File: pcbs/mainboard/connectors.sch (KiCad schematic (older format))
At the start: 10 parts, among them J10 STAT_LED, J11 nReset_Button, J2 key_row_0, J3 key_row_1, J4 key_row_2, J5 ICSP, J6 JTAG, J7 Crank, J8 GPIO, J9 I2C

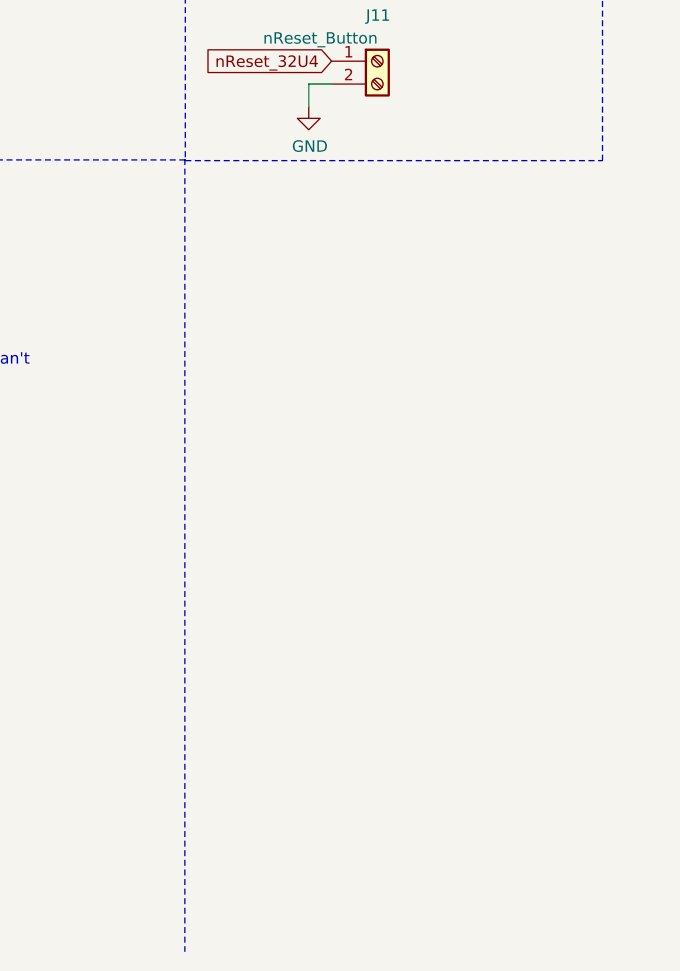
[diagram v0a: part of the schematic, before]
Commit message: Add mounting holes and fix button footprint
Replace button footprint with one which matches the symbol.
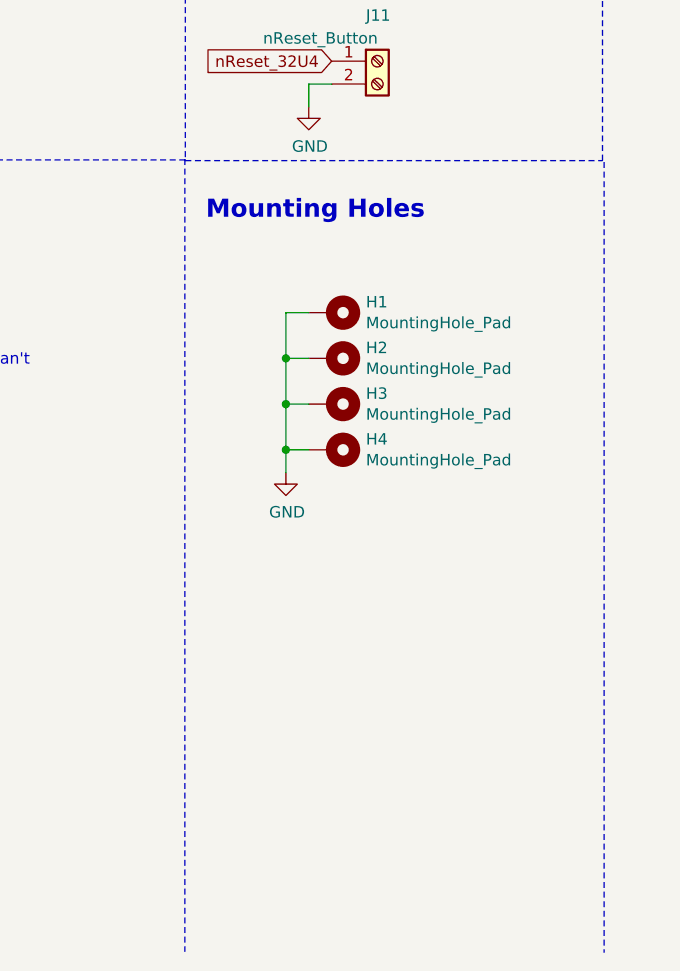
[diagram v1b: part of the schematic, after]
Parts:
- added H1, H2, H3, H4: MountingHole_Pad, MountingHole:MountingHole_3.2mm_M3_Pad_Via, symbol Mechanical:MountingHole_Pad
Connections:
- wire segments 17 -> 25
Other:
- note added: "Mounting Holes"
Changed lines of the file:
@@
 Wire Wire Line
 	1250 6900 1300 6900
+Wire Notes Line
+	4942 4341 4942 7800
+Text Notes 3200 4600 0    79   ~ 16
+Mounting Holes
+$Comp
+L Mechanical:MountingHole_Pad H1
+U 1 1 6153CC4B
+P 3750 5000
+F 0 "H1" V 3704 5150 50  0000 L CNN
+F 1 "MountingHole_Pad" V 3795 5150 50  0000 L CNN
+F 2 "MountingHole:MountingHole_3.2mm_M3_Pad_Via" H 3750 5000 50  0001 C CNN
+F 3 "~" H 3750 5000 50  0001 C CNN
+	1    3750 5000
+	0    1    1    0
+$EndComp
+$Comp
+L Mechanical:MountingHole_Pad H2
+U 1 1 6153E1D0
+P 3750 5200
+F 0 "H2" V 3704 5350 50  0000 L CNN
+F 1 "MountingHole_Pad" V 3795 5350 50  0000 L CNN
+F 2 "MountingHole:MountingHole_3.2mm_M3_Pad_Via" H 3750 5200 50  0001 C CNN
+F 3 "~" H 3750 5200 50  0001 C CNN
+	1    3750 5200
+	0    1    1    0
+$EndComp
+$Comp
+L Mechanical:MountingHole_Pad H3
+U 1 1 6153E50B
+P 3750 5400
+F 0 "H3" V 3704 5550 50  0000 L CNN
+F 1 "MountingHole_Pad" V 3795 5550 50  0000 L CNN
+F 2 "MountingHole:MountingHole_3.2mm_M3_Pad_Via" H 3750 5400 50  0001 C CNN
+F 3 "~" H 3750 5400 50  0001 C CNN
+	1    3750 5400
+	0    1    1    0
+$EndComp
+$Comp
+L Mechanical:MountingHole_Pad H4
+U 1 1 6153E7C0
+P 3750 5600
+F 0 "H4" V 3704 5750 50  0000 L CNN
+F 1 "MountingHole_Pad" V 3795 5750 50  0000 L CNN
+F 2 "MountingHole:MountingHole_3.2mm_M3_Pad_Via" H 3750 5600 50  0001 C CNN
+F 3 "~" H 3750 5600 50  0001 C CNN
+	1    3750 5600
+	0    1    1    0
+$EndComp
+$Comp
+L power:GND #PWR0115
+U 1 1 6153EF14
+P 3550 5700
+F 0 "#PWR0115" H 3550 5450 50  0001 C CNN
+F 1 "GND" H 3555 5527 50  0000 C CNN
+F 2 "" H 3550 5700 50  0001 C CNN
+F 3 "" H 3550 5700 50  0001 C CNN
+	1    3550 5700
+	1    0    0    -1
+$EndComp
+Wire Wire Line
+	3550 5700 3550 5600
+Wire Wire Line
+	3550 5000 3650 5000
+Wire Wire Line
+	3650 5200 3550 5200
+Connection ~ 3550 5200
+Wire Wire Line
+	3550 5200 3550 5000
+Wire Wire Line
+	3550 5400 3650 5400
+Connection ~ 3550 5400
+Wire Wire Line
+	3550 5400 3550 5200
+Wire Wire Line
+	3650 5600 3550 5600
+Connection ~ 3550 5600
+Wire Wire Line
+	3550 5600 3550 5400
 $EndSCHEMATC

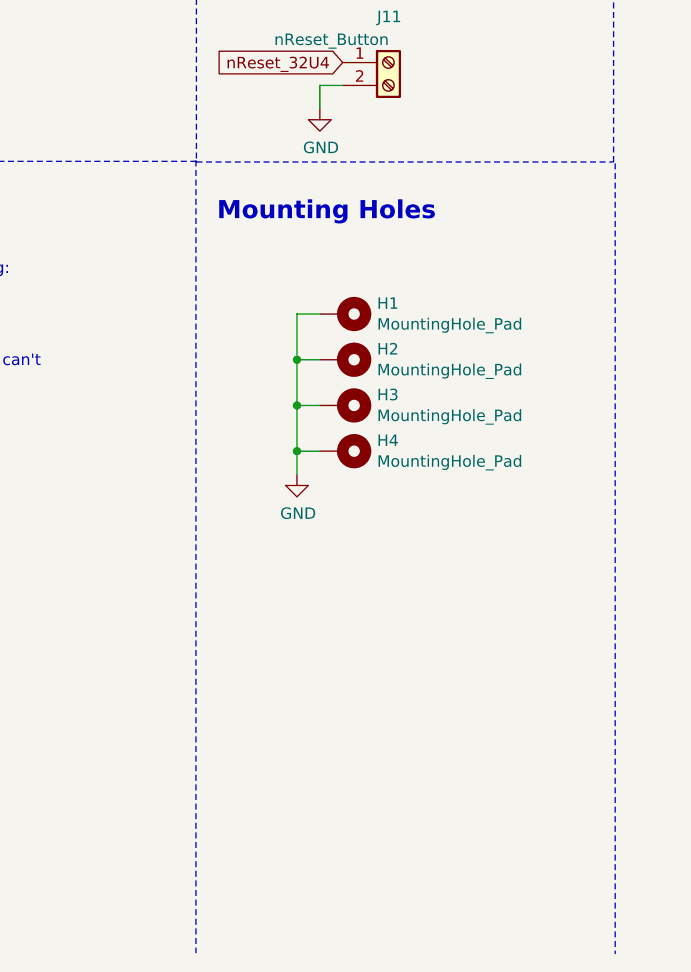
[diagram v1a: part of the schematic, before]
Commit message: Add VBUS screw terminal
Add VBUS screw terminal to allow future subsystems to draw current
from the USB connection, bypassing the small 3V3 regulator.
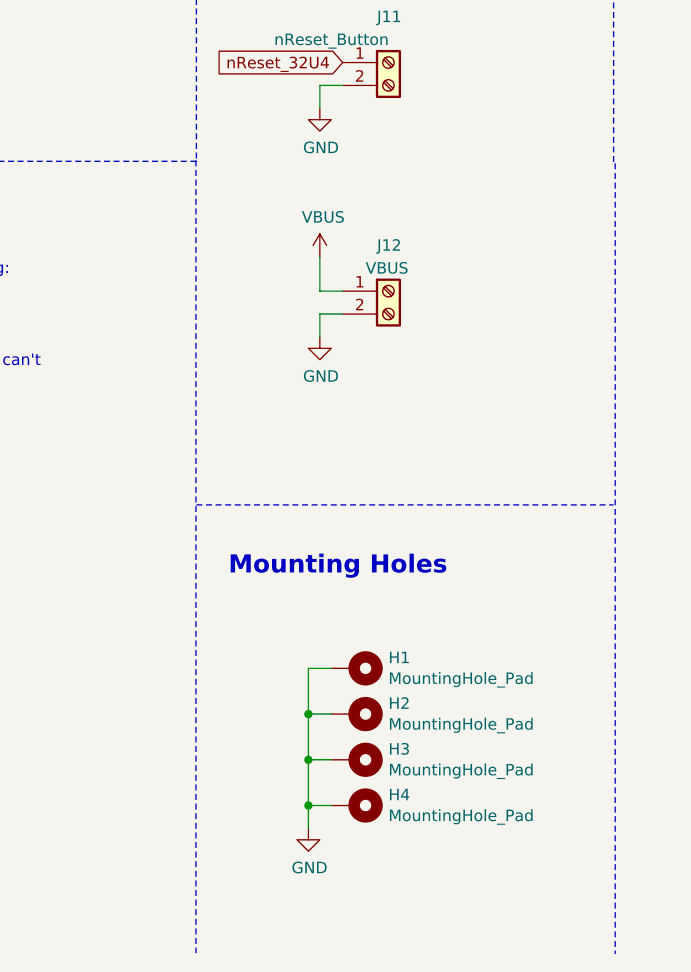
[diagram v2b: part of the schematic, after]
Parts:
- added J12: VBUS, TerminalBlock_Phoenix:TerminalBlock_Phoenix_MKDS-1,5-2-5.08_1x02_P5.08mm_Horizontal, symbol Connector:Screw_Terminal_01x02
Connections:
- net labels added: VBUS
- wire segments 25 -> 29
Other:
- moved on the sheet: H1, H2, H3, H4
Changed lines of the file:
@@
 $EndComp
 Wire Notes Line
-	3110 4335 4935 4335
+	3110 5835 4935 5835
 Wire Notes Line
 	4935 4335 4935 475
@@
 Wire Notes Line
 	4942 4341 4942 7800
-Text Notes 3200 4600 0    79   ~ 16
+Text Notes 3250 6150 0    79   ~ 16
 Mounting Holes
 $Comp
 L Mechanical:MountingHole_Pad H1
 U 1 1 6153CC4B
-P 3750 5000
-F 0 "H1" V 3704 5150 50  0000 L CNN
-F 1 "MountingHole_Pad" V 3795 5150 50  0000 L CNN
-F 2 "MountingHole:MountingHole_3.2mm_M3_Pad_Via" H 3750 5000 50  0001 C CNN
-F 3 "~" H 3750 5000 50  0001 C CNN
-	1    3750 5000
+P 3800 6550
+F 0 "H1" V 3754 6700 50  0000 L CNN
+F 1 "MountingHole_Pad" V 3845 6700 50  0000 L CNN
+F 2 "MountingHole:MountingHole_3.2mm_M3_Pad_Via" H 3800 6550 50  0001 C CNN
+F 3 "~" H 3800 6550 50  0001 C CNN
+	1    3800 6550
 	0    1    1    0
 $EndComp
@@
 L Mechanical:MountingHole_Pad H2
 U 1 1 6153E1D0
-P 3750 5200
-F 0 "H2" V 3704 5350 50  0000 L CNN
-F 1 "MountingHole_Pad" V 3795 5350 50  0000 L CNN
-F 2 "MountingHole:MountingHole_3.2mm_M3_Pad_Via" H 3750 5200 50  0001 C CNN
-F 3 "~" H 3750 5200 50  0001 C CNN
-	1    3750 5200
+P 3800 6750
+F 0 "H2" V 3754 6900 50  0000 L CNN
+F 1 "MountingHole_Pad" V 3845 6900 50  0000 L CNN
+F 2 "MountingHole:MountingHole_3.2mm_M3_Pad_Via" H 3800 6750 50  0001 C CNN
+F 3 "~" H 3800 6750 50  0001 C CNN
+	1    3800 6750
 	0    1    1    0
 $EndComp
@@
 L Mechanical:MountingHole_Pad H3
 U 1 1 6153E50B
-P 3750 5400
-F 0 "H3" V 3704 5550 50  0000 L CNN
-F 1 "MountingHole_Pad" V 3795 5550 50  0000 L CNN
-F 2 "MountingHole:MountingHole_3.2mm_M3_Pad_Via" H 3750 5400 50  0001 C CNN
-F 3 "~" H 3750 5400 50  0001 C CNN
-	1    3750 5400
+P 3800 6950
+F 0 "H3" V 3754 7100 50  0000 L CNN
+F 1 "MountingHole_Pad" V 3845 7100 50  0000 L CNN
+F 2 "MountingHole:MountingHole_3.2mm_M3_Pad_Via" H 3800 6950 50  0001 C CNN
+F 3 "~" H 3800 6950 50  0001 C CNN
+	1    3800 6950
 	0    1    1    0
 $EndComp
@@
 L Mechanical:MountingHole_Pad H4
 U 1 1 6153E7C0
-P 3750 5600
-F 0 "H4" V 3704 5750 50  0000 L CNN
-F 1 "MountingHole_Pad" V 3795 5750 50  0000 L CNN
-F 2 "MountingHole:MountingHole_3.2mm_M3_Pad_Via" H 3750 5600 50  0001 C CNN
-F 3 "~" H 3750 5600 50  0001 C CNN
-	1    3750 5600
+P 3800 7150
+F 0 "H4" V 3754 7300 50  0000 L CNN
+F 1 "MountingHole_Pad" V 3845 7300 50  0000 L CNN
+F 2 "MountingHole:MountingHole_3.2mm_M3_Pad_Via" H 3800 7150 50  0001 C CNN
+F 3 "~" H 3800 7150 50  0001 C CNN
+	1    3800 7150
 	0    1    1    0
 $EndComp
@@
 L power:GND #PWR0115
 U 1 1 6153EF14
-P 3550 5700
-F 0 "#PWR0115" H 3550 5450 50  0001 C CNN
-F 1 "GND" H 3555 5527 50  0000 C CNN
-F 2 "" H 3550 5700 50  0001 C CNN
-F 3 "" H 3550 5700 50  0001 C CNN
-	1    3550 5700
-	1    0    0    -1
-$EndComp
-Wire Wire Line
-	3550 5700 3550 5600
-Wire Wire Line
-	3550 5000 3650 5000
-Wire Wire Line
-	3650 5200 3550 5200
-Connection ~ 3550 5200
-Wire Wire Line
-	3550 5200 3550 5000
-Wire Wire Line
-	3550 5400 3650 5400
-Connection ~ 3550 5400
-Wire Wire Line
-	3550 5400 3550 5200
-Wire Wire Line
-	3650 5600 3550 5600
-Connection ~ 3550 5600
-Wire Wire Line
-	3550 5600 3550 5400
+P 3600 7250
+F 0 "#PWR0115" H 3600 7000 50  0001 C CNN
+F 1 "GND" H 3605 7077 50  0000 C CNN
+F 2 "" H 3600 7250 50  0001 C CNN
+F 3 "" H 3600 7250 50  0001 C CNN
+	1    3600 7250
+	1    0    0    -1
+$EndComp
+Wire Wire Line
+	3600 7250 3600 7150
+Wire Wire Line
+	3600 6550 3700 6550
+Wire Wire Line
+	3700 6750 3600 6750
+Connection ~ 3600 6750
+Wire Wire Line
+	3600 6750 3600 6550
+Wire Wire Line
+	3600 6950 3700 6950
+Connection ~ 3600 6950
+Wire Wire Line
+	3600 6950 3600 6750
+Wire Wire Line
+	3700 7150 3600 7150
+Connection ~ 3600 7150
+Wire Wire Line
+	3600 7150 3600 6950
+Wire Wire Line
+	3650 5000 3750 5000
+Wire Wire Line
+	3650 5100 3650 5000
+$Comp
+L power:GND #PWR0116
+U 1 1 61620CEB
+P 3650 5100
+F 0 "#PWR0116" H 3650 4850 50  0001 C CNN
+F 1 "GND" H 3655 4927 50  0000 C CNN
+F 2 "" H 3650 5100 50  0001 C CNN
+F 3 "" H 3650 5100 50  0001 C CNN
+	1    3650 5100
+	1    0    0    -1
+$EndComp
+$Comp
+L Connector:Screw_Terminal_01x02 J12
+U 1 1 61620CF5
+P 3950 4900
+F 0 "J12" H 3900 5100 50  0000 L CNN
+F 1 "VBUS" H 3850 5000 50  0000 L CNN
+F 2 "TerminalBlock_Phoenix:TerminalBlock_Phoenix_MKDS-1,5-2-5.08_1x02_P5.08mm_Horizontal" H 3950 4900 50  0001 C CNN
+F 3 "~" H 3950 4900 50  0001 C CNN
+	1    3950 4900
+	1    0    0    -1
+$EndComp
+$Comp
+L power:VBUS #PWR0117
+U 1 1 616267BA
+P 3650 4750
+F 0 "#PWR0117" H 3650 4600 50  0001 C CNN
+F 1 "VBUS" H 3665 4923 50  0000 C CNN
+F 2 "" H 3650 4750 50  0001 C CNN
+F 3 "" H 3650 4750 50  0001 C CNN
+	1    3650 4750
+	1    0    0    -1
+$EndComp
+Wire Wire Line
+	3650 4750 3650 4900
+Wire Wire Line
+	3650 4900 3750 4900
 $EndSCHEMATC

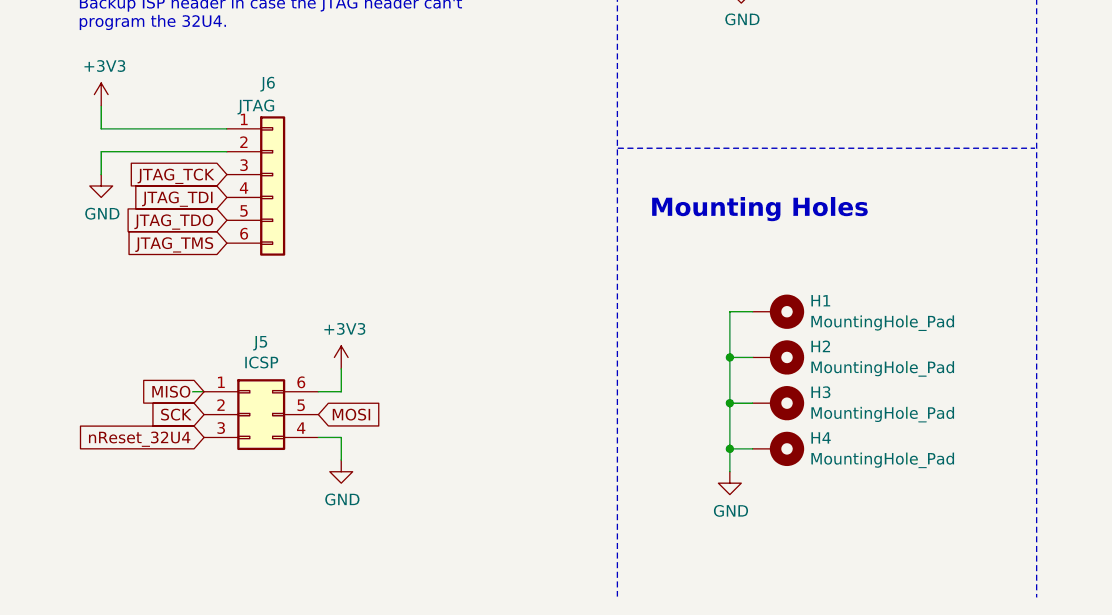
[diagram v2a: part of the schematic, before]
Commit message: Add first draft of mainboard layout
Change pinout of XC95 to better link to the key_row screw terminals.

Change ordering of some signals on screw terminals and JTAG header
to allow more sensible routing.

Revise mounting hole scheme to only place one between the two rows
of terminal blocks rather than at each corner on the top.
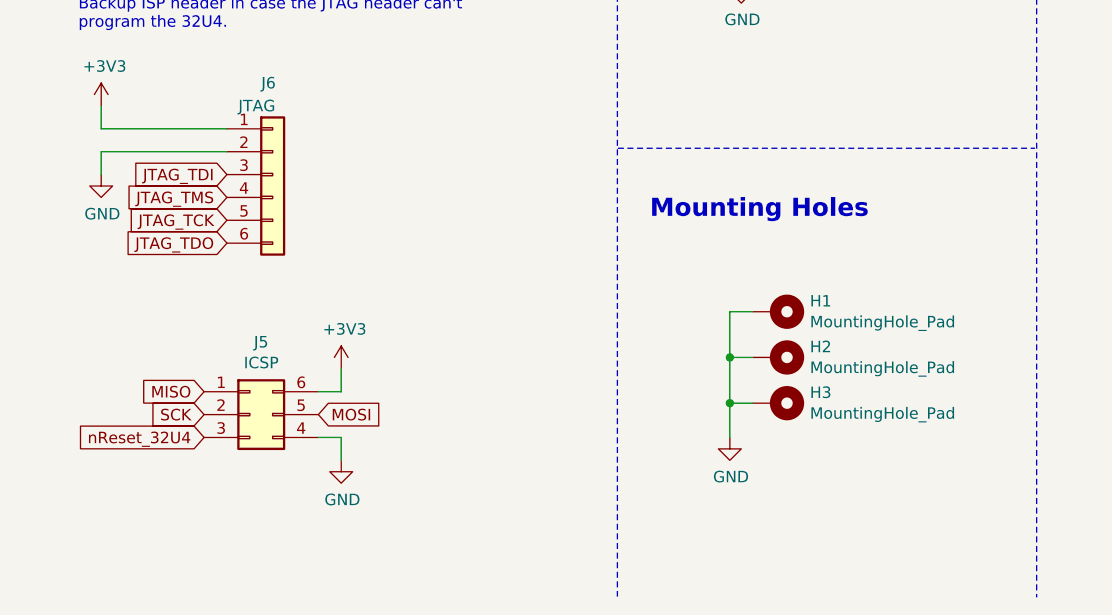
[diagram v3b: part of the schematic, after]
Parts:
- removed H4: MountingHole_Pad, MountingHole:MountingHole_3.2mm_M3_Pad_Via, symbol Mechanical:MountingHole_Pad
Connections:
- wire segments 29 -> 26
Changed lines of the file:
@@
 Wire Wire Line
 	850  5750 1400 5750
+Text GLabel 1400 6150 0    50   Input ~ 0
+JTAG_TCK
 Text GLabel 1400 5950 0    50   Input ~ 0
-JTAG_TCK
+JTAG_TDI
+Text GLabel 1400 6250 0    50   Input ~ 0
+JTAG_TDO
 Text GLabel 1400 6050 0    50   Input ~ 0
-JTAG_TDI
-Text GLabel 1400 6150 0    50   Input ~ 0
-JTAG_TDO
-Text GLabel 1400 6250 0    50   Input ~ 0
 JTAG_TMS
 Text GLabel 1300 7100 0    50   Input ~ 0
@@
 	1    0    0    -1
 $EndComp
-Wire Wire Line
-	1250 6900 1300 6900
 Wire Notes Line
 	4942 4341 4942 7800
@@
 $EndComp
 $Comp
-L Mechanical:MountingHole_Pad H4
-U 1 1 6153E7C0
-P 3800 7150
-F 0 "H4" V 3754 7300 50  0000 L CNN
-F 1 "MountingHole_Pad" V 3845 7300 50  0000 L CNN
-F 2 "MountingHole:MountingHole_3.2mm_M3_Pad_Via" H 3800 7150 50  0001 C CNN
-F 3 "~" H 3800 7150 50  0001 C CNN
-	1    3800 7150
-	0    1    1    0
-$EndComp
-$Comp
 L power:GND #PWR0115
 U 1 1 6153EF14
-P 3600 7250
-F 0 "#PWR0115" H 3600 7000 50  0001 C CNN
-F 1 "GND" H 3605 7077 50  0000 C CNN
-F 2 "" H 3600 7250 50  0001 C CNN
-F 3 "" H 3600 7250 50  0001 C CNN
-	1    3600 7250
-	1    0    0    -1
-$EndComp
-Wire Wire Line
-	3600 7250 3600 7150
+P 3600 7100
+F 0 "#PWR0115" H 3600 6850 50  0001 C CNN
+F 1 "GND" H 3605 6927 50  0000 C CNN
+F 2 "" H 3600 7100 50  0001 C CNN
+F 3 "" H 3600 7100 50  0001 C CNN
+	1    3600 7100
+	1    0    0    -1
+$EndComp
 Wire Wire Line
 	3600 6550 3700 6550
@@
 Wire Wire Line
 	3600 6950 3600 6750
-Wire Wire Line
-	3700 7150 3600 7150
-Connection ~ 3600 7150
-Wire Wire Line
-	3600 7150 3600 6950
 Wire Wire Line
 	3650 5000 3750 5000
@@
 Wire Wire Line
 	3650 4900 3750 4900
+Wire Wire Line
+	3600 6950 3600 7100
 $EndSCHEMATC

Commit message: Add useful/readabhle silkscreen
Swap pins on CRANK_V_IN terminal block to shorten track
and match the polarity of other +/- terminal blocks.
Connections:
- net CRANK_V_IN: now also J7.2 (Pin_2); no longer J7.1 (Pin_1)
- net GND: now also J7.1 (Pin_1); no longer J7.2 (Pin_2)
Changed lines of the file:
@@
 	1    0    0    -1
 $EndComp
-Text GLabel 2500 1250 0    50   Input ~ 0
+Text GLabel 2350 1350 0    50   Input ~ 0
 CRANK_V_IN
-Wire Wire Line
-	2500 1350 2400 1350
-Wire Wire Line
-	2400 1350 2400 1450
 $Comp
 L power:GND #PWR0103
@@
 Wire Wire Line
 	3600 6950 3600 7100
+Wire Wire Line
+	2400 1250 2500 1250
+Wire Wire Line
+	2400 1250 2400 1450
+Wire Wire Line
+	2350 1350 2500 1350
 $EndSCHEMATC
